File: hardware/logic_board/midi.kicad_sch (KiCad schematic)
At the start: 10 parts, among them J1 MIDI In, J1 MIDI_IO, J2 MIDI Thru

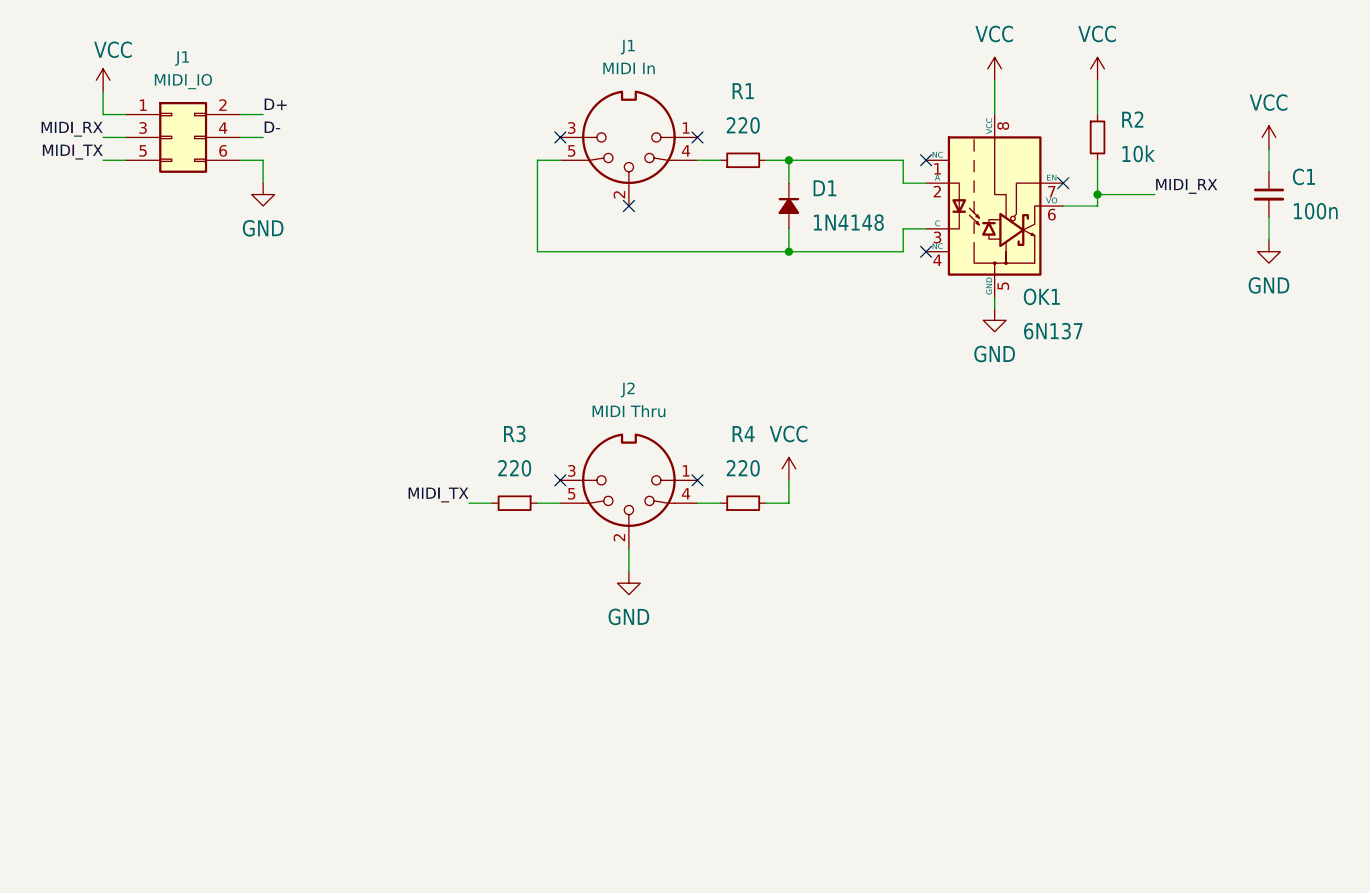
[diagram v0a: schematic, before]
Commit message: move all logic components to daughterboard, move MIDI to new board
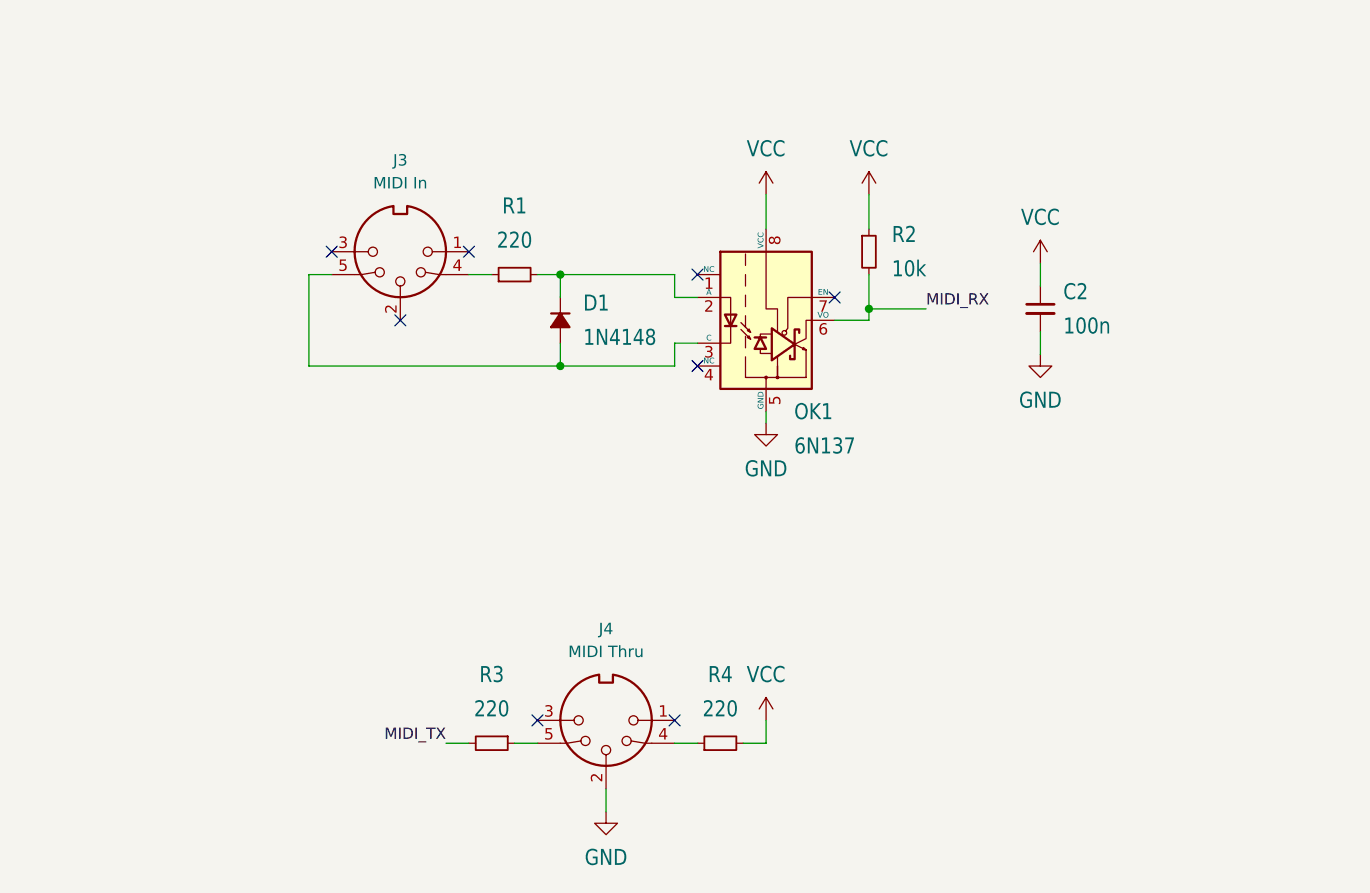
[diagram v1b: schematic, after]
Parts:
- removed C1: 100n, shruthi_control_board_xt_v03:C025-024X044, symbol Device:C_Small
- removed J1: MIDI_IO, Connector_IDC:IDC-Header_2x05_P2.54mm_Vertical, symbol Connector_Generic:Conn_02x03_Odd_Even
- removed J1: MIDI In, symbol Connector:DIN-5_180degree
- removed J2: MIDI Thru, symbol Connector:DIN-5_180degree
- added C2: 100n, shruthi_control_board_xt_v03:C025-024X044, symbol Device:C_Small
- added J3: MIDI In, symbol Connector:DIN-5_180degree
- added J4: MIDI Thru, symbol Connector:DIN-5_180degree
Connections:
- net GND: now also C2.2, J4.2
- net VCC: now also C2.1
- net at R1.1: now also J3.4
- net at R3.1: now also J4.5
- net at D1.2 (A), OK1.3 (C): now also J3.5
- net at R4.1: now also J4.4
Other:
- moved on the sheet: D1, OK1, R1, R2, R3, R4
